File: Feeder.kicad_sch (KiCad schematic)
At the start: 50 parts, among them T502 CMB1670V, U702 TPS562202, U710 TPS562202

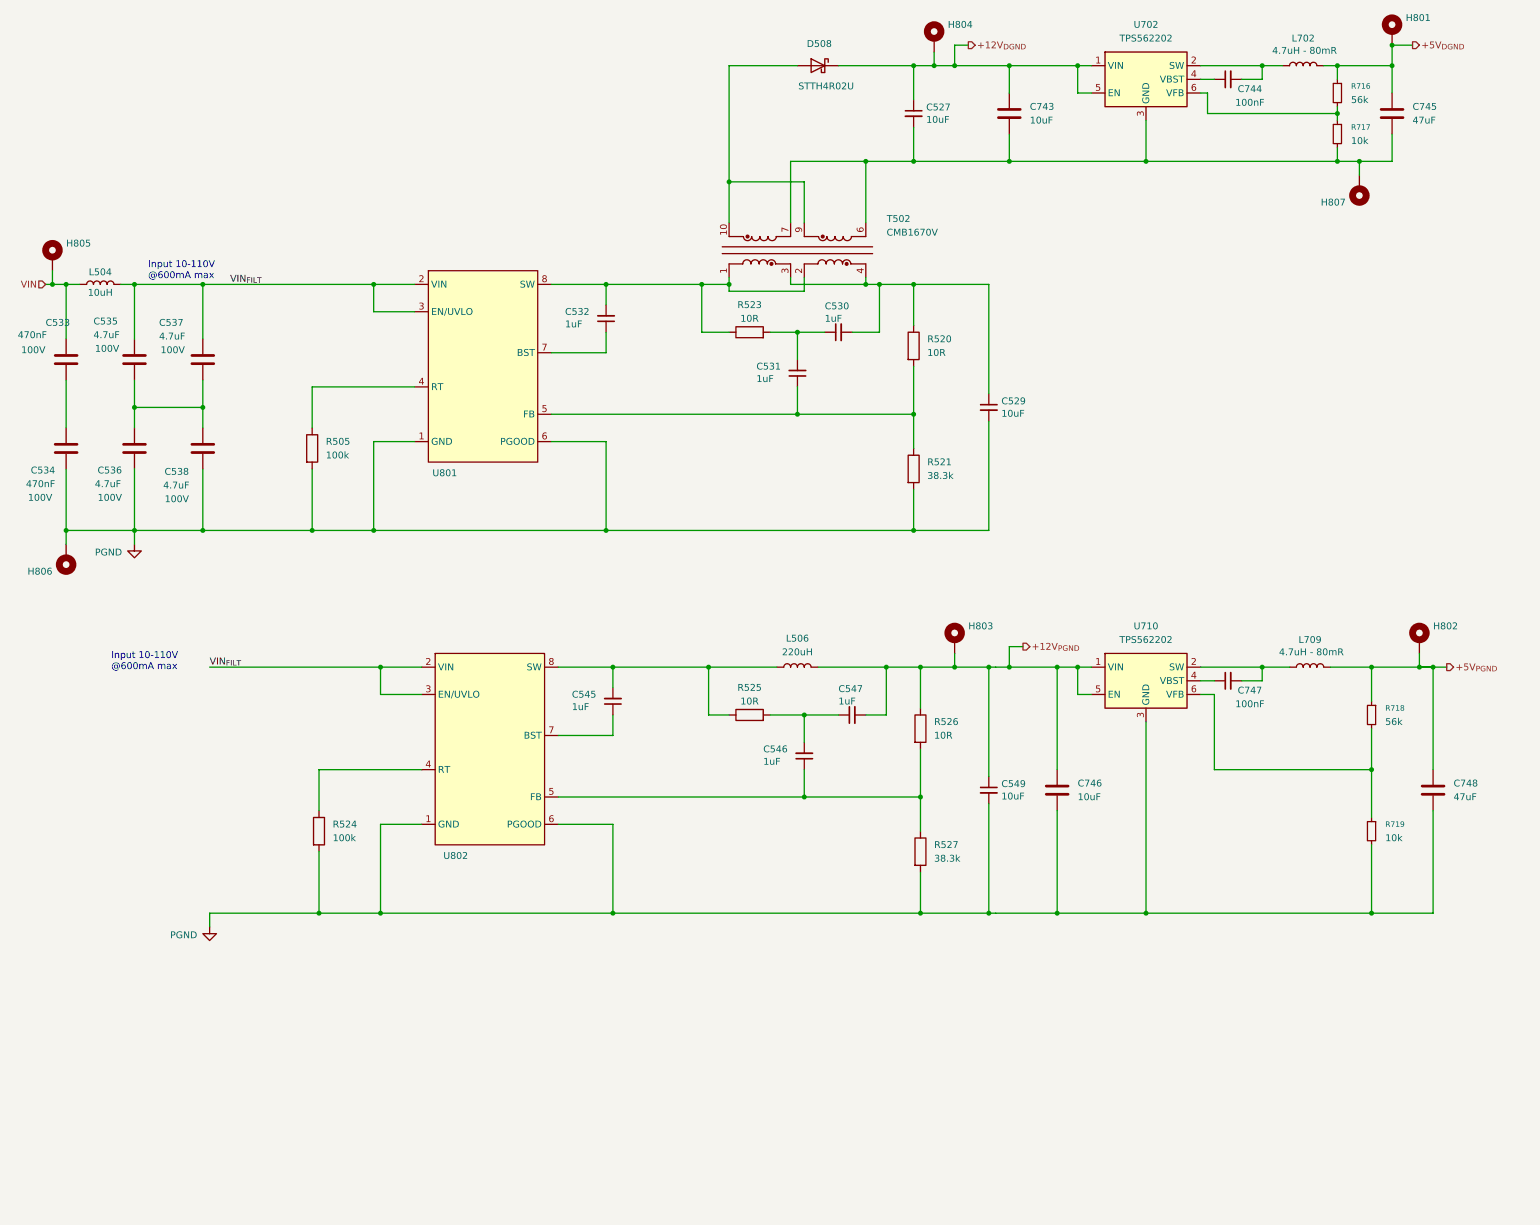
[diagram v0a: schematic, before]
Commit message: Adding the placeholder for the capacitor board.
Signed-off-by: Jean Alinei <jean.alinei@owntech.org>
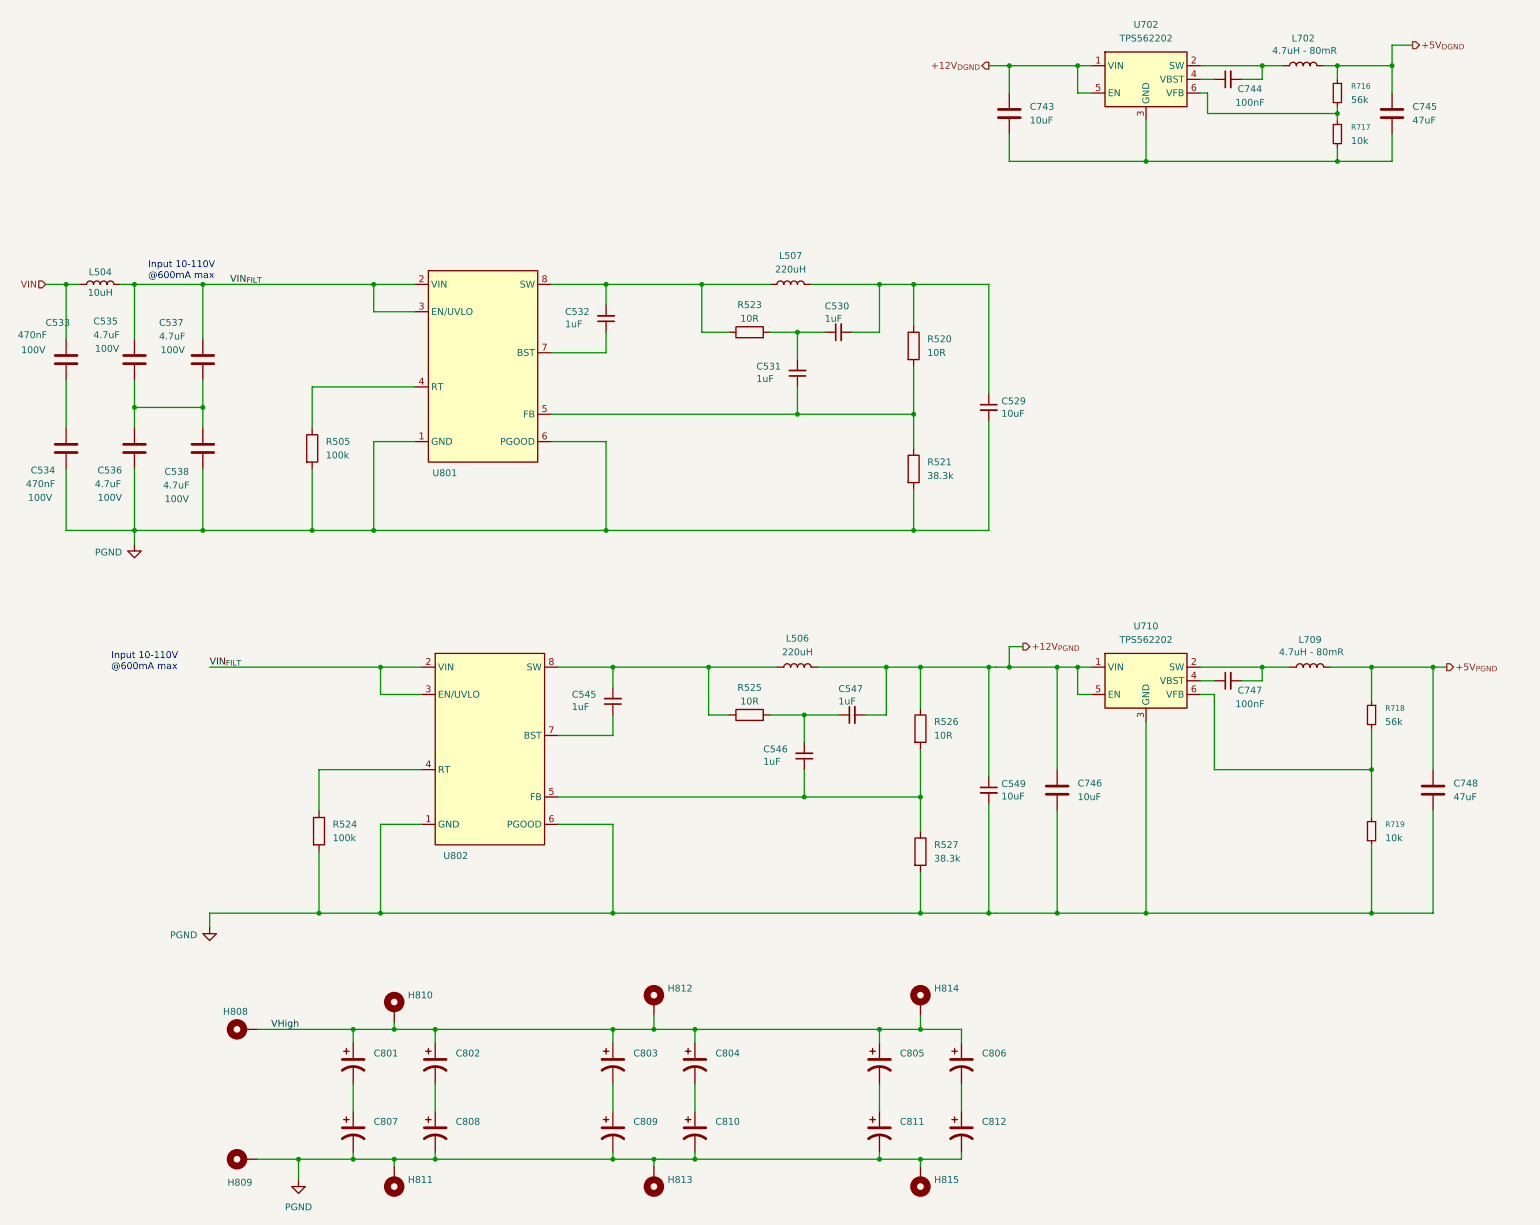
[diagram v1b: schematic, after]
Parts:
- removed C527: 10uF, Footprints:C_1210_3225Metric, symbol Device:C_Small
- removed D508: STTH4R02U, Diode_SMD:D_SMB, symbol Device:D_Schottky
- removed H801, H802, H803, H804, H805, H806, H807: MountingHole_Pad, MountingHole:MountingHole_2.2mm_M2_Pad_Via, symbol Mechanical:MountingHole_Pad
- removed T502: CMB1670V, Footprints:PA2467NL, symbol Symbols:CMB1670V
- added C801, C802, C803, C804, C805, C806, C807, C808, C809, C810, C811, C812: C_Polarized_US, Capacitor_SMD:CP_Elec_10x12.6, symbol Device:C_Polarized_US
- added H808, H809, H810, H811, H812, H813, H814, H815: MountingHole_Pad, MountingHole:MountingHole_3.2mm_M3_Pad_Via, symbol Mechanical:MountingHole_Pad
- added L507: 220uH, Footprints:L-SMD_L10.5-W10.3_SLD10D50, symbol Device:L
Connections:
- net PGND: now also C807.2, C808.2, C809.2, C810.2, C811.2, C812.2, H809.1, H811.1, H813.1, H815.1
- net at C532.2, R523.1, U801.8 (SW): now also L507.1
- net at C529.1, C530.2, R520.1: now also L507.2
- new net: C801.2, C807.1
- new net: C802.2, C808.1
- new net: C806.2, C812.1
- new net: C803.2, C809.1
- new net: C805.2, C811.1
- new net: C804.2, C810.1
- new net VHigh: C801.1, C802.1, C803.1, C804.1, C805.1, C806.1, H808.1, H810.1, H812.1, H814.1

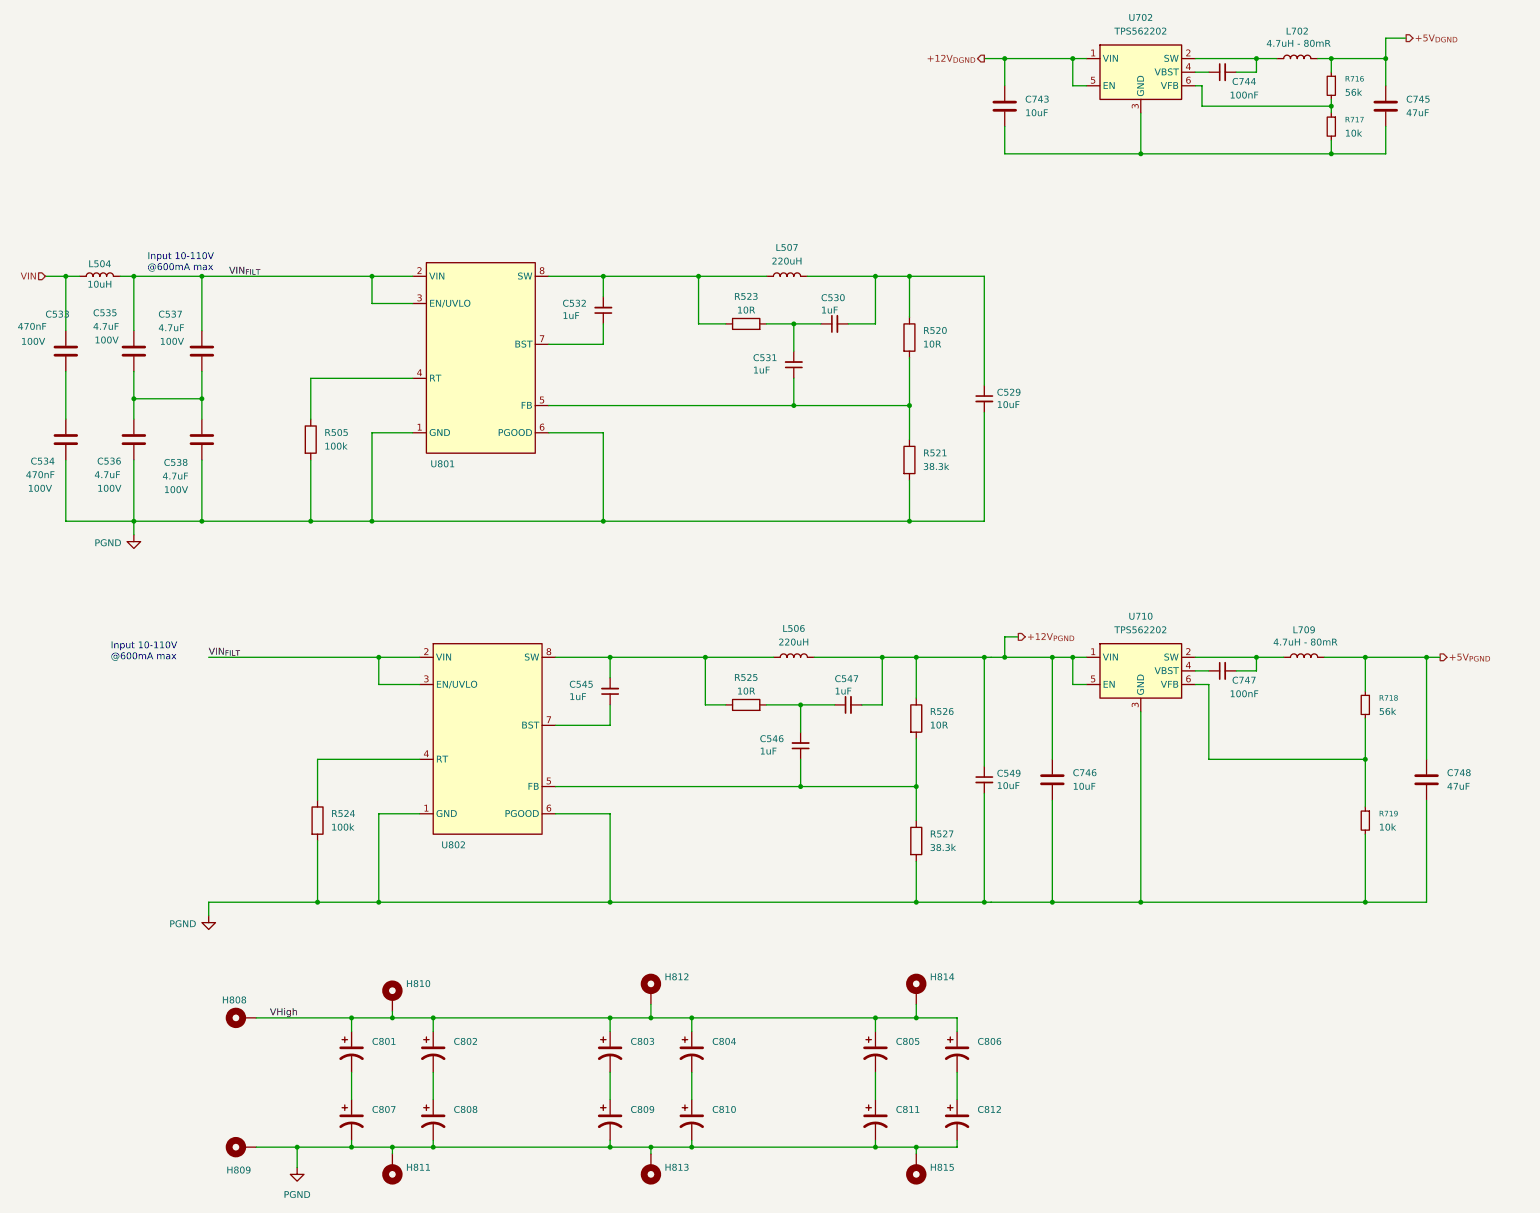
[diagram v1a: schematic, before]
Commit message: v0 of the capacitor and feeder board
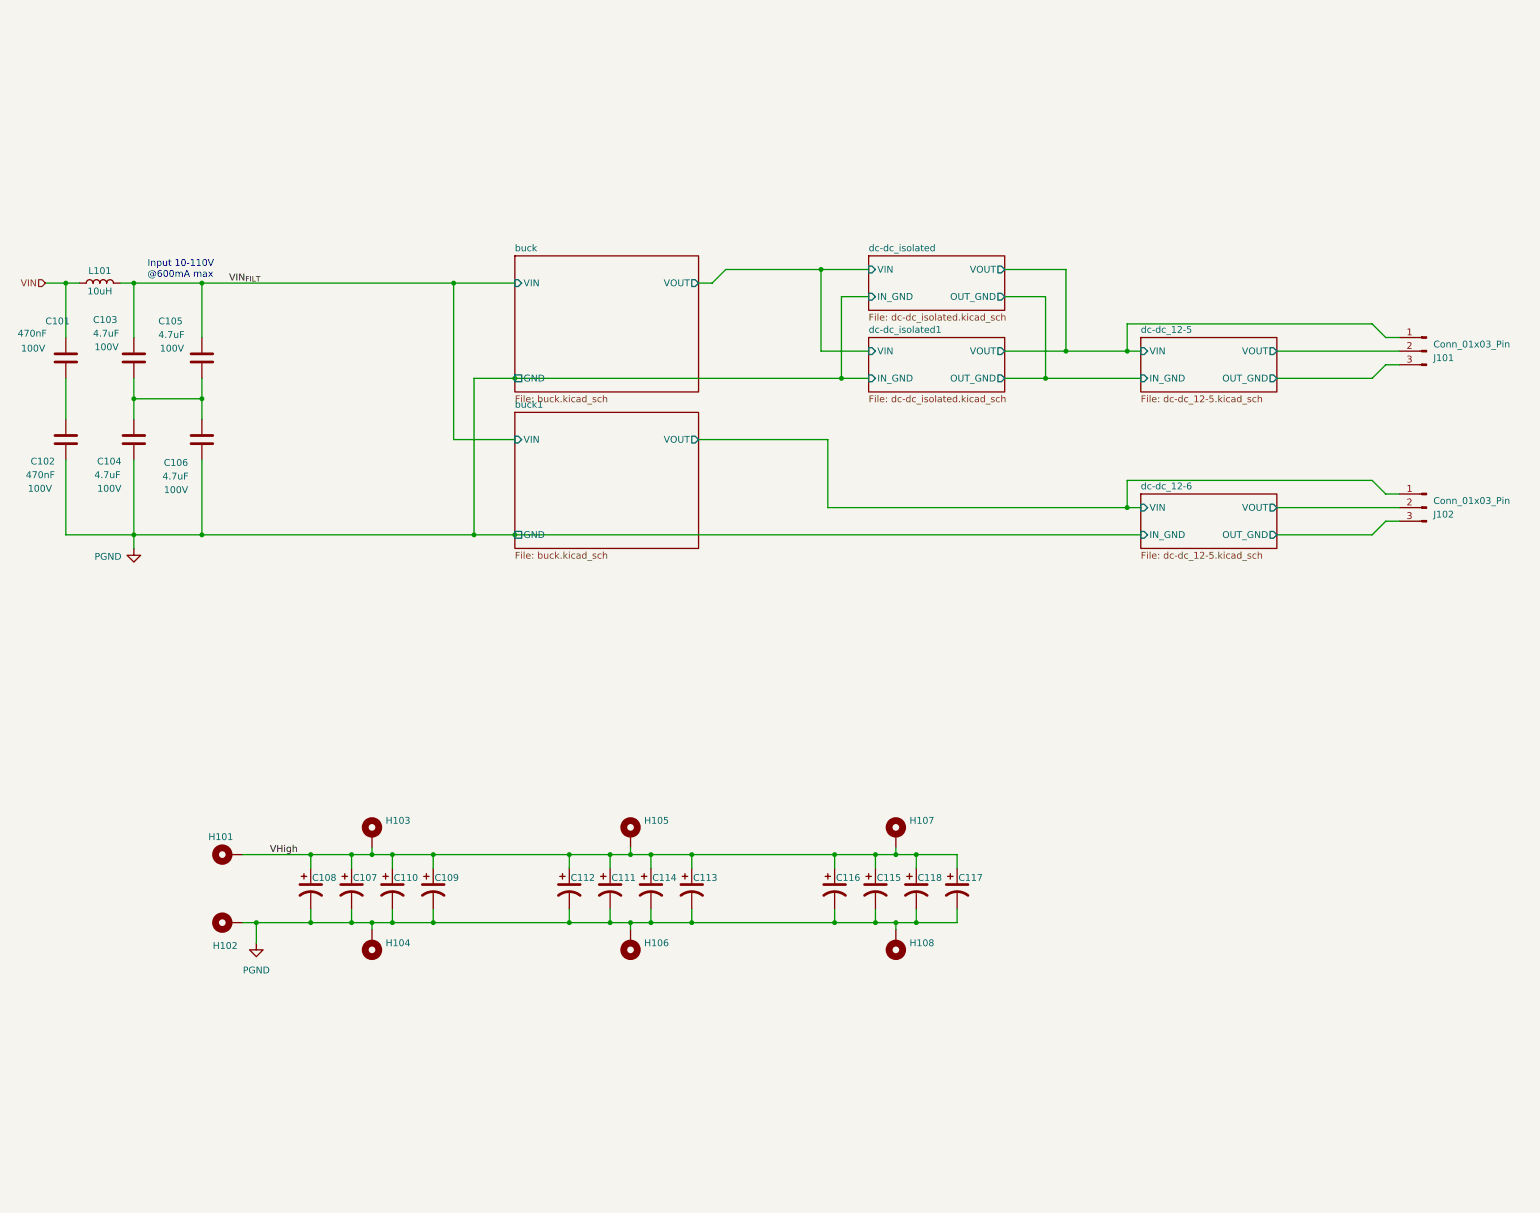
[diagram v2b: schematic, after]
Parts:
- removed C529, C549: 10uF, Footprints:C_1210_3225Metric, symbol Device:C_Small
- removed C530, C531, C532, C545, C546, C547: 1uF, Footprints:C_0805_2012Metric, symbol Device:C_Small
- removed C743, C746: 10uF, Capacitor_SMD:C_0805_2012Metric, symbol Device:C
- removed C744, C747: 100nF, Capacitor_SMD:C_0805_2012Metric, symbol Device:C_Small
- removed C745, C748: 47uF, Capacitor_SMD:C_1206_3216Metric, symbol Device:C
- removed L506, L507: 220uH, Footprints:L-SMD_L10.5-W10.3_SLD10D50, symbol Device:L
- removed L702, L709: 4.7uH - 80mR, Inductor_SMD:L_Cenker_CKCS4020, symbol Device:L
- removed R505, R524: 100k, Footprints:R_0805_2012Metric, symbol Device:R
- removed R520, R523, R525, R526: 10R, Footprints:R_0805_2012Metric, symbol Device:R
- removed R521, R527: 38.3k, Footprints:R_0805_2012Metric, symbol Device:R
- removed R716, R718: 56k, Footprints:R_0805_2012Metric, symbol Device:R_Small
- removed R717, R719: 10k, Footprints:R_0805_2012Metric, symbol Device:R_Small
- removed U702, U710: TPS562202, Package_TO_SOT_SMD:SOT-563, symbol Regulator_Switching:TPS562202
- removed U801, U802: (no value), Package_SO:Texas_R-PDSO-G8_EP2.95x4.9mm_Mask2.4x3.1mm_ThermalVias, symbol Symbols:LM5169
- added J101, J102: Conn_01x03_Pin, Connector_PinHeader_2.54mm:PinHeader_1x03_P2.54mm_Vertical, symbol Connector:Conn_01x03_Pin
- renumbered C533 to C101, C534 to C102, C535 to C103, C536 to C104, C537 to C105, C538 to C106, C801 to C107, C807 to C108, C802 to C109, C808 to C110, C803 to C111, C809 to C112, C804 to C113, C810 to C114, C805 to C115, C811 to C116, C806 to C117, C812 to C118, H808 to H101, H809 to H102, H810 to H103, H811 to H104, H812 to H105, H813 to H106, H814 to H107, H815 to H108, L504 to L101
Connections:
- net PGND: now also C107.2, C109.2, C111.2, C113.2, C115.2, C117.2
- net VHigh: now also C108.1, C110.1, C112.1, C114.1, C116.1, C118.1
- new net buck1/VOUT: J102.1 (Pin_1)
- new net dc-dc_12-5/OUT_GND: J101.3 (Pin_3)
- new net dc-dc_12-5/VIN: J101.1 (Pin_1)
- new net dc-dc_12-5/VOUT: J101.2 (Pin_2)
- new net dc-dc_12-6/OUT_GND: J102.3 (Pin_3)
- new net dc-dc_12-6/VOUT: J102.2 (Pin_2)
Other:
- added sheet buck (buck.kicad_sch)
- added sheet buck1 (buck.kicad_sch)
- added sheet dc-dc_12-5 (dc-dc_12-5.kicad_sch)
- added sheet dc-dc_12-6 (dc-dc_12-5.kicad_sch)
- added sheet dc-dc_isolated (dc-dc_isolated.kicad_sch)
- added sheet dc-dc_isolated1 (dc-dc_isolated.kicad_sch)
- moved on the sheet: C101, C103, C105, C107, C108, C109, C110, C111, C112, C113, C114, C115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

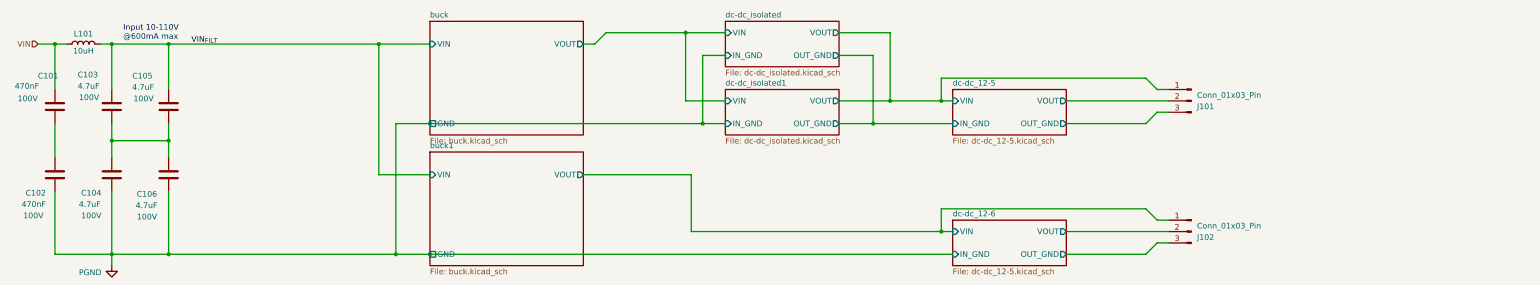
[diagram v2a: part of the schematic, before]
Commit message: added eeprom and isolation slots
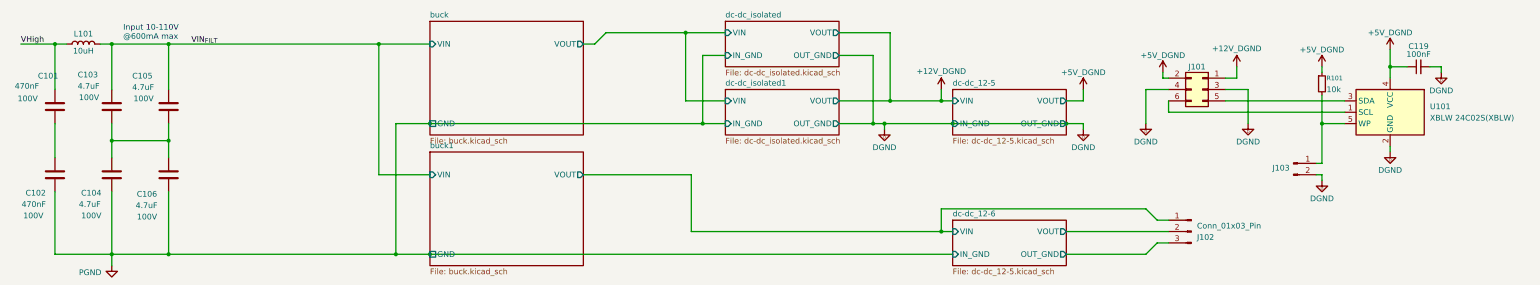
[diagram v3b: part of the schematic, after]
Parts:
- removed J101: Conn_01x03_Pin, Connector_PinHeader_2.54mm:PinHeader_1x03_P2.54mm_Vertical, symbol Connector:Conn_01x03_Pin
- added C119: 100nF, Capacitor_SMD:C_0603_1608Metric, symbol Device:C_Small
- added J101: Conn_02x03_Odd_Even, Connector_PinHeader_2.54mm:PinHeader_2x03_P2.54mm_Vertical, symbol Connector_Generic:Conn_02x03_Odd_Even
- added J103: Conn_01x02_Pin, Connector_PinHeader_2.54mm:PinHeader_1x02_P2.54mm_Vertical, symbol Connector:Conn_01x02_Pin
- added R101: 10k, Capacitor_SMD:C_0603_1608Metric, symbol Device:R_Small
- added U101: XBLW 24C02S(XBLW), Package_TO_SOT_SMD:SOT-23-5, symbol Memory_EEPROM:AT24CS02-STUM
- J102: footprint Connector_PinHeader_2.54mm:PinHeader_1x03_P2.54mm_Vertical -> (none)
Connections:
- net VIN is gone; now on net VHigh: C101.1, L101.1
- new net: J101.6 (Pin_6), U101.1 (SCL)
- new net: J101.5 (Pin_5), U101.3 (SDA)
- new net: J103.1 (Pin_1), R101.2, U101.5 (WP)
- new net +12V_DGND: J101.1 (Pin_1)
- new net +5V_DGND: C119.1, J101.2 (Pin_2), R101.1, U101.4 (VCC)
- new net DGND: C119.2, J101.3 (Pin_3), J101.4 (Pin_4), J103.2 (Pin_2), U101.2 (GND)
